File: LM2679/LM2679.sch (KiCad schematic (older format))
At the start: 15 parts, among them J1 INPUT, J2 OUTPUT, U1 LM2679SX-5.0/NOPB

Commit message: Updates to schematic and PCB
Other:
- note added: "Buck Regulator"
- note added: "Input: 11.8 - 13.8VDC\nInput(I): 2.24A\nOutput: 5V (5A max.)\nƒ(sw): 260kHz"
- note added: "Mounting Holes"
- moved on the sheet: C1, C2, C3, C4, C5, D1, H1, H2, H3, H4, J1, J2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

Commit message: Changes to PCB footprints
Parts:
- C1: footprint Capacitor_SMD:CP_Elec_8.3x8.3_Panasonic_M -> Capacitor_SMD:CP_Elec_8.3x8.3_Panasonic_SVPF_E7
- C5: footprint Capacitor_SMD:CP_Elec_10.3x10.3_Panasonic_M -> Capacitor_SMD:CP_Elec_10.3x10.3_Panasonic_SVPF_F12
- D1: footprint Package_TO_SOT_SMD:TO-263-2_TabPin1 -> Package_TO_SOT_SMD:TO-263-2_TabPin1_HandSoldering
- U1: footprint Package_TO_SOT_SMD:TO-263-7_TabPin8 -> Package_TO_SOT_SMD:TO-263-7_TabPin8_HandSoldering
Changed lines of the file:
@@
 Sheet 1 1
 Title "Urban Garden MKII – Buck Regulator SMD"
-Date "2021-05-03"
-Rev "0.0.1"
+Date "2021-05-05"
+Rev "0.0.2"
 Comp "u/ergeha"
 Comment1 ""
@@
 F 0 "C1" H 3715 3871 50  0000 L CNN
 F 1 "180µF " H 3715 3780 50  0000 L CNN
-F 2 "Capacitor_SMD:CP_Elec_8.3x8.3_Panasonic_M" H 3830 3682 50  0001 C CNN
+F 2 "Capacitor_SMD:CP_Elec_8.3x8.3_Panasonic_SVPF_E7" H 3830 3682 50  0001 C CNN
 F 3 "https://industrial.panasonic.com/ww/products/capacitors/polymer-capacitors/os-con/models/20SVPF180M" H 3830 3682 50  0001 C CNN
 F 4 "20V" H 3715 3697 39  0000 L CNN "Rating"
@@
 F 0 "U1" H 5400 3750 50  0000 C CNN
 F 1 "LM2679SX-5.0/NOPB" H 5400 3650 50  0000 C CNN
-F 2 "Package_TO_SOT_SMD:TO-263-7_TabPin8" H 5900 3450 50  0001 C CNN
+F 2 "Package_TO_SOT_SMD:TO-263-7_TabPin8_HandSoldering" H 5900 3450 50  0001 C CNN
 F 3 "https://www.ti.com/lit/ds/symlink/lm2679.pdf?ts=1619264190615" H 5900 3450 50  0001 C CNN
 F 4 "LM2679SX-5.0/NOPB" H 5900 3350 50  0001 C CNN "MPN"
@@
 F 0 "D1" V 6754 3830 50  0000 L CNN
 F 1 "850mV @ 20A" V 6845 3830 50  0000 L CNN
-F 2 "Package_TO_SOT_SMD:TO-263-2_TabPin1" H 6800 3750 50  0001 C CNN
+F 2 "Package_TO_SOT_SMD:TO-263-2_TabPin1_HandSoldering" H 6800 3750 50  0001 C CNN
 F 3 "https://www.st.com/content/ccc/resource/technical/document/datasheet/group2/8f/d3/41/ea/82/b2/4b/5a/CD00228904/files/CD00228904.pdf/jcr:content/translations/en.CD00228904.pdf" H 6800 3750 50  0001 C CNN
 F 4 "STPS20M100SG-TR" H 6800 3750 50  0001 C CNN "MPN"
@@
 F 0 "C5" H 7915 3871 50  0000 L CNN
 F 1 "330µF " H 7915 3780 50  0000 L CNN
-F 2 "Capacitor_SMD:CP_Elec_10.3x10.3_Panasonic_M" H 8030 3682 50  0001 C CNN
+F 2 "Capacitor_SMD:CP_Elec_10.3x10.3_Panasonic_SVPF_F12" H 8030 3682 50  0001 C CNN
 F 3 "https://industrial.panasonic.com/ww/products/capacitors/polymer-capacitors/os-con/models/16SVP330M" H 8030 3682 50  0001 C CNN
 F 4 "16V" H 7915 3697 39  0000 L CNN "Rating"

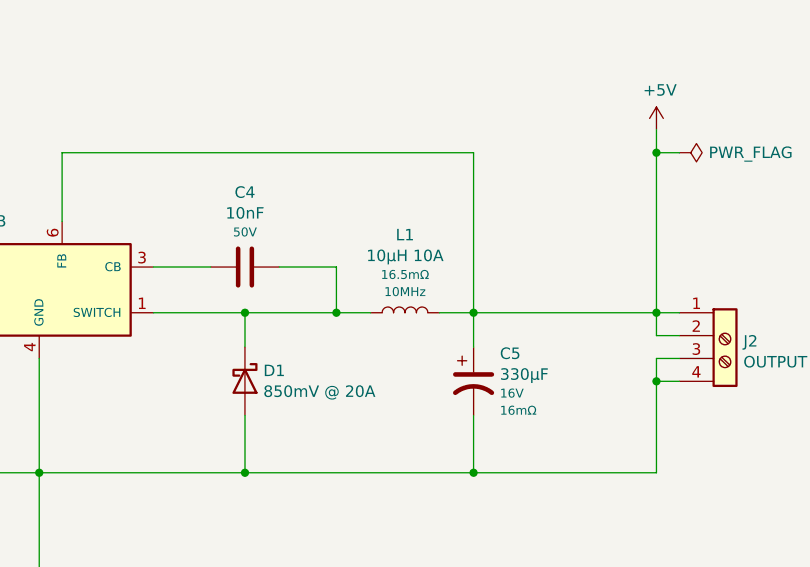
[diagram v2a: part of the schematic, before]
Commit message: Inductor changed
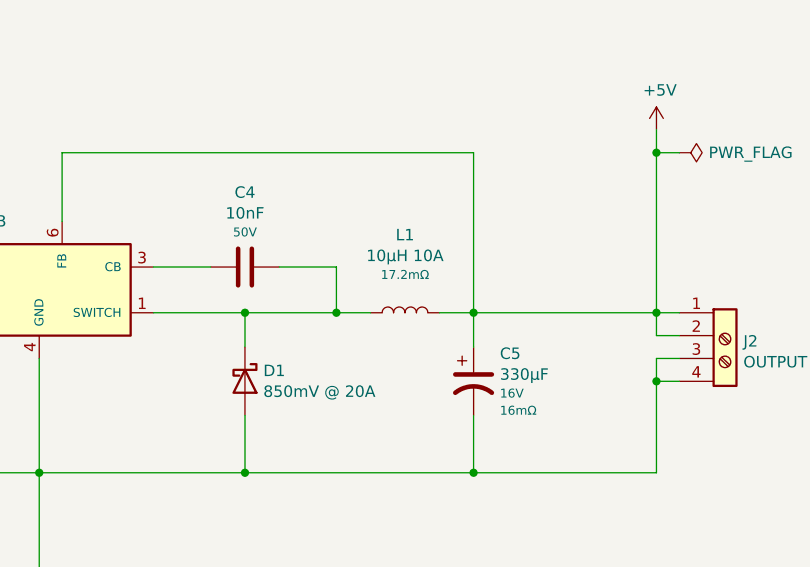
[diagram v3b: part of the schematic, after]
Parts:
- L1: footprint Inductor_SMD:L_Bourns_SRP1245A -> Inductor_SMD:L_Vishay_IHLP-5050_HandSolder; DCR 16.5mΩ -> 17.2mΩ; MPN SRP1265A-100M -> IHLP5050FDER100M01; Manufacturer Bourns Inc. -> Vishay Dale; SRF 10MHz -> (none)
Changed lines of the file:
@@
 F 0 "L1" H 7500 3790 50  0000 C CNN
 F 1 "10µH 10A" H 7500 3699 50  0000 C CNN
-F 2 "Inductor_SMD:L_Bourns_SRP1245A" V 7500 3450 50  0001 C CNN
-F 3 "https://www.bourns.com/docs/Product-Datasheets/SRP1265A.pdf" V 7500 3450 50  0001 C CNN
-F 4 "16.5mΩ" H 7500 3616 39  0000 C CNN "DCR"
-F 5 "10MHz" H 7500 3541 39  0000 C CNN "SRF"
-F 6 "SRP1265A-100M" H 7500 3450 50  0001 C CNN "MPN"
-F 7 "Bourns Inc." H 7500 3450 50  0001 C CNN "Manufacturer"
+F 2 "Inductor_SMD:L_Vishay_IHLP-5050_HandSolder" V 7500 3450 50  0001 C CNN
+F 3 "https://www.vishay.com/docs/34123/ihlp-5050fd-01.pdf" V 7500 3450 50  0001 C CNN
+F 4 "17.2mΩ" H 7500 3616 39  0000 C CNN "DCR"
+F 5 "~" H 7500 3541 39  0000 C CNN "SRF"
+F 6 "IHLP5050FDER100M01" H 7500 3450 50  0001 C CNN "MPN"
+F 7 "Vishay Dale" H 7500 3450 50  0001 C CNN "Manufacturer"
 F 8 "~" H 7500 3450 50  0001 C CNN "Impedence "
 F 9 "~" H 7500 3450 50  0001 C CNN "Power"
@@
 F 9 "~" H 5200 3750 50  0001 C CNN "Impedence "
 F 10 "~" H 5200 3750 50  0001 C CNN "Rating"
-F 11 "" H 5200 3750 50  0001 C CNN "SRF"
+F 11 "~" H 5200 3750 50  0001 C CNN "SRF"
 	1    5200 3750
 	1    0    0    -1
